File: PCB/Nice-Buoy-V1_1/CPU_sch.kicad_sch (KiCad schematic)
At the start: 53 parts, among them J101 1051330011, J102 LEDSTRIP, J102 SW1, J102 SW2, J901 Display, Q8 2N7002, Q9 2N7002, SW3 ~{BOOT}, SW4 ~{RESET}, U101 SRV05-4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

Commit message: HarwareV1.0 frozen Software version 1.1 V1.0 frozen
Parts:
- J102: LCSC C144394 -> C161870
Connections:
- net +5V: no longer C50.2, U102.7 (REGIN), U102.8 (VBUS)
- net at D9.2 (A), J101.1 (VBUS), U101.5 (VP): now also C50.2, U102.7 (REGIN), U102.8 (VBUS)
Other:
- moved on the sheet: D9

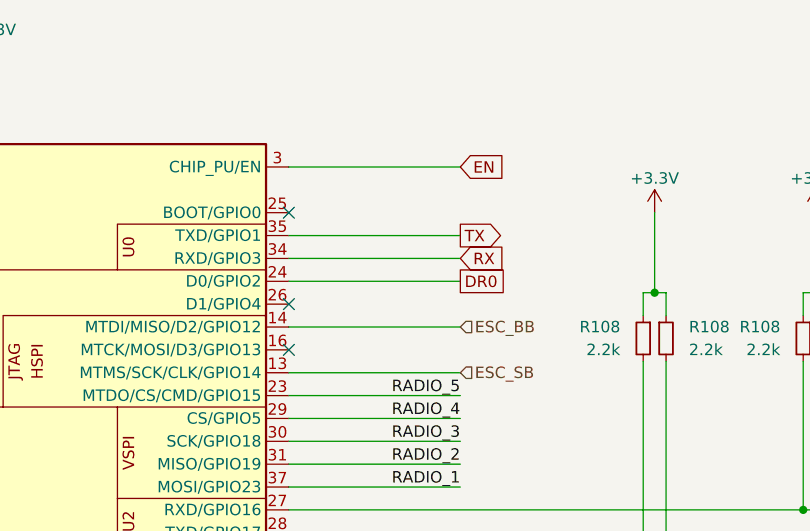
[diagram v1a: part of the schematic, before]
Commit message: settingup V1.1 software. Compasso ok dispay ok gps ok
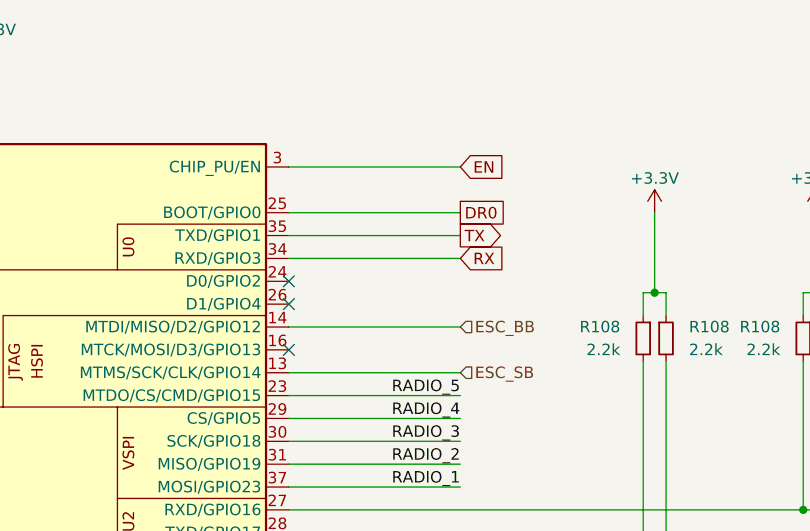
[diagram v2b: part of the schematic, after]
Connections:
- net DR0: now also U103.25 (BOOT/GPIO0); no longer U103.24 (D0/GPIO2)
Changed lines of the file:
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@@
   (no_connect (at 201.93 60.96))
   (no_connect (at 128.27 163.83))
-  (no_connect (at 201.93 50.8))
+  (no_connect (at 201.93 58.42))
   (no_connect (at 128.27 168.91))
   (no_connect (at 97.79 158.75))
@@
     (stroke (width 0) (type default))
   )
-  (wire (pts (xy 220.98 58.42) (xy 201.93 58.42))
+  (wire (pts (xy 220.98 50.8) (xy 201.93 50.8))
     (stroke (width 0) (type default))
   )
@@
     )
   )
-  (global_label "DR0" (shape passive) (at 220.98 58.42 0) (fields_autoplaced)
-    (effects (font (size 1.27 1.27)) (justify left))
-    (property "Intersheetrefs" "${INTERSHEET_REFS}" (at 226.108 58.42 0)
-      (effects (font (size 1.27 1.27)) (justify left) hide)
-    )
+  (global_label "DR0" (shape passive) (at 220.98 50.8 0) (fields_autoplaced)
+    (effects (font (size 1.27 1.27)) (justify left))
+    (property "Intersheetrefs" "${INTERSHEET_REFS}" (at 226.108 50.8 0)
+      (effects (font (size 1.27 1.27)) (justify left) hide)
+    )
